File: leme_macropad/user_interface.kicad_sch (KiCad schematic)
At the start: 31 parts, among them J1 OLED display, SW1 SW_Push, SW2 SW_Push, SW3 SW_Push, SW4 RotaryEncoder_Switch, SW5 SW_Push, SW6 SW_Push, SW7 SW_Push, SW8 SW_Push, SW9 SW_Push

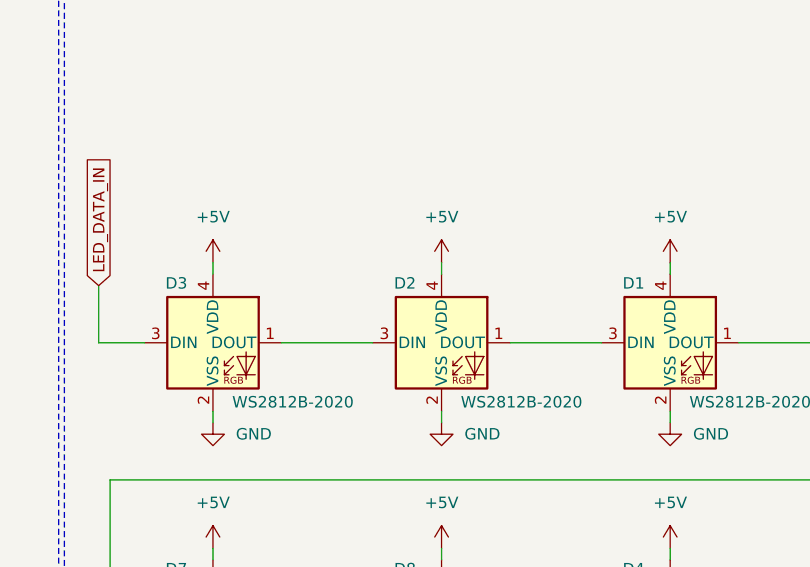
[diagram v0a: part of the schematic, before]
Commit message: Reorders ws2812 LEDs
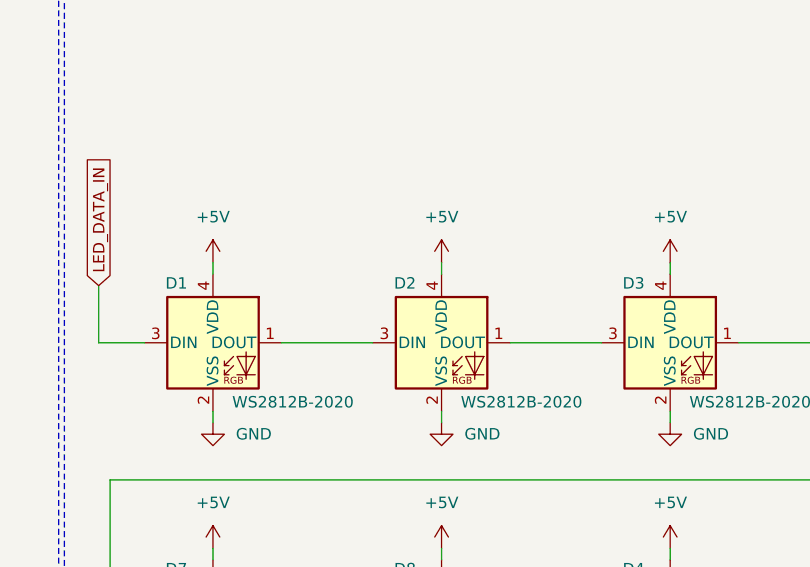
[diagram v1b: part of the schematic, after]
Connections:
- net LED_DATA_IN: now also D1.3 (DIN); no longer D3.3 (DIN)
- net at D3.1 (DOUT): now also D6.3 (DIN); no longer D2.3 (DIN)
- net at D1.1 (DOUT): now also D2.3 (DIN); no longer D6.3 (DIN)
- net at D2.1 (DOUT): now also D3.3 (DIN); no longer D1.3 (DIN)
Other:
- moved on the sheet: D1, D3
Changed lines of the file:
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@@
 	(symbol
 		(lib_id "LED:WS2812B-2020")
-		(at 190.5 63.5 0)
+		(at 241.3 63.5 0)
 		(unit 1)
 		(exclude_from_sim no)
@@
 		(dnp no)
 		(property "Reference" "D3"
-			(at 186.436 56.896 0)
+			(at 237.236 56.896 0)
 			(effects
 				(font
@@
 		)
 		(property "Value" "WS2812B-2020"
-			(at 199.39 70.104 0)
+			(at 250.19 70.104 0)
 			(effects
 				(font
@@
 		)
 		(property "Footprint" "LED_SMD:LED_WS2812B-2020_PLCC4_2.0x2.0mm"
-			(at 191.77 71.12 0)
+			(at 242.57 71.12 0)
 			(effects
 				(font
@@
 		)
 		(property "Datasheet" "https://cdn-shop.adafruit.com/product-files/4684/4684_WS2812B-2020_V1.3_EN.pdf"
-			(at 193.04 73.025 0)
+			(at 243.84 73.025 0)
 			(effects
 				(font
@@
 		)
 		(property "Description" "RGB LED with integrated controller, 2.0 x 2.0 mm, 12 mA"
-			(at 190.5 63.5 0)
+			(at 241.3 63.5 0)
 			(effects
 				(font
@@
 	(symbol
 		(lib_id "LED:WS2812B-2020")
-		(at 241.3 63.5 0)
+		(at 190.5 63.5 0)
 		(unit 1)
 		(exclude_from_sim no)
@@
 		(dnp no)
 		(property "Reference" "D1"
-			(at 237.236 56.896 0)
+			(at 186.436 56.896 0)
 			(effects
 				(font
@@
 		)
 		(property "Value" "WS2812B-2020"
-			(at 250.19 70.104 0)
+			(at 199.39 70.104 0)
 			(effects
 				(font
@@
 		)
 		(property "Footprint" "LED_SMD:LED_WS2812B-2020_PLCC4_2.0x2.0mm"
-			(at 242.57 71.12 0)
+			(at 191.77 71.12 0)
 			(effects
 				(font
@@
 		)
 		(property "Datasheet" "https://cdn-shop.adafruit.com/product-files/4684/4684_WS2812B-2020_V1.3_EN.pdf"
-			(at 243.84 73.025 0)
+			(at 193.04 73.025 0)
 			(effects
 				(font
@@
 		)
 		(property "Description" "RGB LED with integrated controller, 2.0 x 2.0 mm, 12 mA"
-			(at 241.3 63.5 0)
-			(effects
-				(font
+			(at 190.5 63.5 0)
+			(effects
+				(font

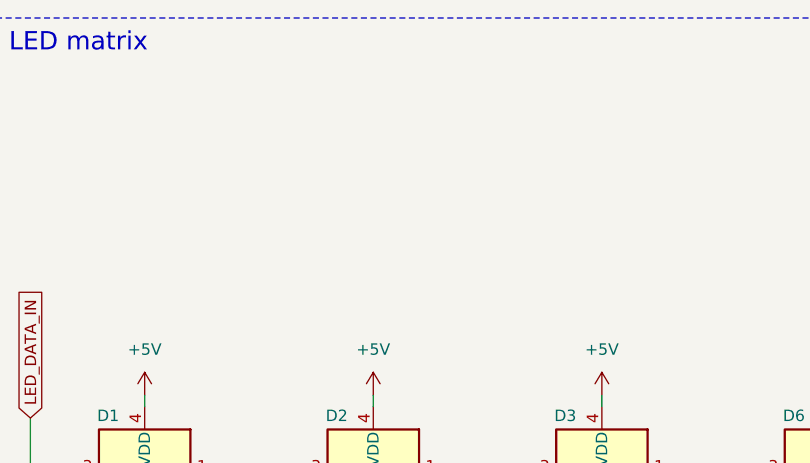
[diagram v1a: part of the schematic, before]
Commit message: Adds pull-up resistor footprint (component marked as DNP) to the LED data line
QMK has a open-drain WS2812 driver[1], which we can potentially use to
drive the LEDs at 5V. The issue is that, in theory, the RP2040 is not 5V
tolerant, and the QMK docs are very specific about this needing to be
the case. That's why the component is marked as "Do Not Populate", and
we'll leave the footprint there for experimentation.

[1]: https://docs.qmk.fm/drivers/ws2812#open-drain-circuit
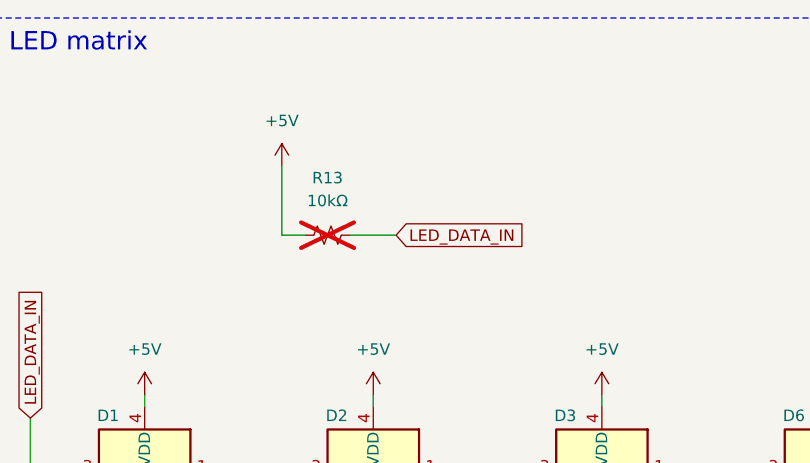
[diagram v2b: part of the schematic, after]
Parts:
- added R13: 10kΩ, Resistor_SMD:R_0402_1005Metric_Pad0.72x0.64mm_HandSolder, symbol Device:R_Small_US
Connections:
- net +5V: now also R13.1
- net LED_DATA_IN: now also R13.2
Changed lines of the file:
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@@
 	(wire
 		(pts
+			(xy 205.74 36.83) (xy 208.28 36.83)
+		)
+		(stroke
+			(width 0)
+			(type default)
+		)
+	)
+	(wire
+		(pts
 			(xy 60.96 95.25) (xy 87.63 95.25)
 		)
@@
 	(wire
 		(pts
+			(xy 205.74 29.21) (xy 205.74 36.83)
+		)
+		(stroke
+			(width 0)
+			(type default)
+		)
+	)
+	(wire
+		(pts
 			(xy 95.25 172.72) (xy 100.33 172.72)
 		)
@@
 	(wire
 		(pts
+			(xy 213.36 36.83) (xy 218.44 36.83)
+		)
+		(stroke
+			(width 0)
+			(type default)
+		)
+	)
+	(wire
+		(pts
 			(xy 60.96 115.57) (xy 63.5 115.57)
 		)
@@
 		)
 	)
+	(global_label "LED_DATA_IN"
+		(shape input)
+		(at 218.44 36.83 0)
+		(fields_autoplaced yes)
+		(effects
+			(font
+				(size 1.27 1.27)
+			)
+			(justify left)
+		)
+		(property "Intersheetrefs" "${INTERSHEET_REFS}"
+			(at 233.1576 36.83 0)
+			(effects
+				(font
+					(size 1.27 1.27)
+				)
+				(justify left)
+				(hide yes)
+			)
+		)
+	)
 	(global_label "I2C0_SDA"
 		(shape input)
@@
 	)
 	(symbol
+		(lib_id "power:+5V")
+		(at 205.74 29.21 0)
+		(unit 1)
+		(exclude_from_sim no)
+		(in_bom yes)
+		(on_board yes)
+		(dnp no)
+		(fields_autoplaced yes)
+		(property "Reference" "#PWR062"
+			(at 205.74 33.02 0)
+			(effects
+				(font
+					(size 1.27 1.27)
+				)
+				(hide yes)
+			)
+		)
+		(property "Value" "+5V"
+			(at 205.74 24.13 0)
+			(effects
+				(font
+					(size 1.27 1.27)
+				)
+			)
+		)
+		(property "Footprint" ""
+			(at 205.74 29.21 0)
+			(effects
+				(font
+					(size 1.27 1.27)
+				)
+				(hide yes)
+			)
+		)
+		(property "Datasheet" ""
+			(at 205.74 29.21 0)
+			(effects
+				(font
+					(size 1.27 1.27)
+				)
+				(hide yes)
+			)
+		)
+		(property "Description" "Power symbol creates a global label with name \"+5V\""
+			(at 205.74 29.21 0)
+			(effects
+				(font
+					(size 1.27 1.27)
+				)
+				(hide yes)
+			)
+		)
+		(pin "1"
+		)
+		(instances
+			(project "leme_macropad"
+				(path "/a37365a2-c635-4451-9354-78f9e753d687/b6fad1bd-9b8b-42cb-b41f-ac701051e19c"
+					(reference "#PWR062")
+					(unit 1)
+				)
+			)
+		)
+	)
+	(symbol
 		(lib_id "Device:D_Small")
 		(at 34.29 90.17 90)
@@
 					(unit 1)
 				)
+			)
+		)
+	)
+	(symbol
+		(lib_id "Device:R_Small_US")
+		(at 210.82 36.83 90)
+		(unit 1)
+		(exclude_from_sim no)
+		(in_bom yes)
+		(on_board yes)
+		(dnp yes)
+		(fields_autoplaced yes)
+		(property "Reference" "R13"
+			(at 210.82 30.48 90)
+			(effects
+				(font
+					(size 1.27 1.27)
+				)
+			)
+		)
+		(property "Value" "10kΩ"
+			(at 210.82 33.02 90)
+			(effects
+				(font
+					(size 1.27 1.27)
+				)
+			)
+		)
+		(property "Footprint" "Resistor_SMD:R_0402_1005Metric_Pad0.72x0.64mm_HandSolder"
+			(at 210.82 36.83 0)
+			(effects
+				(font
+					(size 1.27 1.27)
+				)
+				(hide yes)
+			)
+		)
+		(property "Datasheet" "~"
+			(at 210.82 36.83 0)
+			(effects
+				(font
+					(size 1.27 1.27)
+				)
+				(hide yes)
+			)
+		)
+		(property "Description" "Resistor, small US symbol"
+			(at 210.82 36.83 0)
+			(effects
+				(font
+					(size 1.27 1.27)
+				)
+				(hide yes)
+			)
+		)
+		(pin "1"
+		)
+		(pin "2"
+		)
+		(instances
+			(project "leme_macropad"
+				(path "/a37365a2-c635-4451-9354-78f9e753d687/b6fad1bd-9b8b-42cb-b41f-ac701051e19c"
+					(reference "R13")
+					(unit 1)
+				)

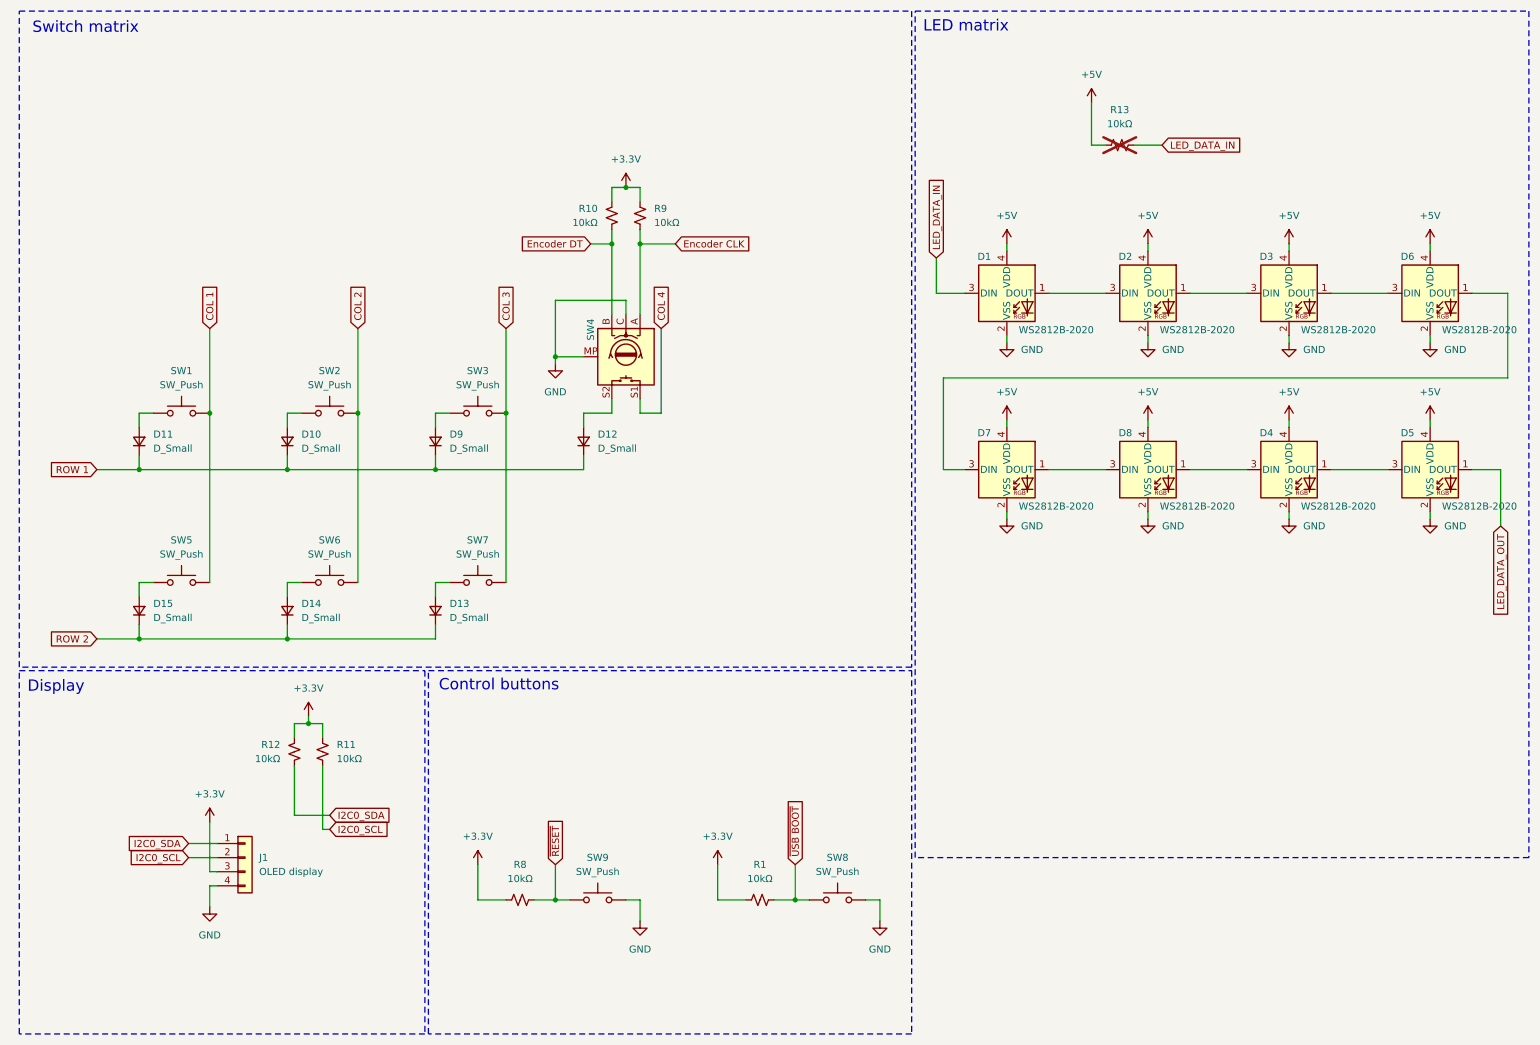
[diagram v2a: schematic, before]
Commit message: Geographically reanotates component designators
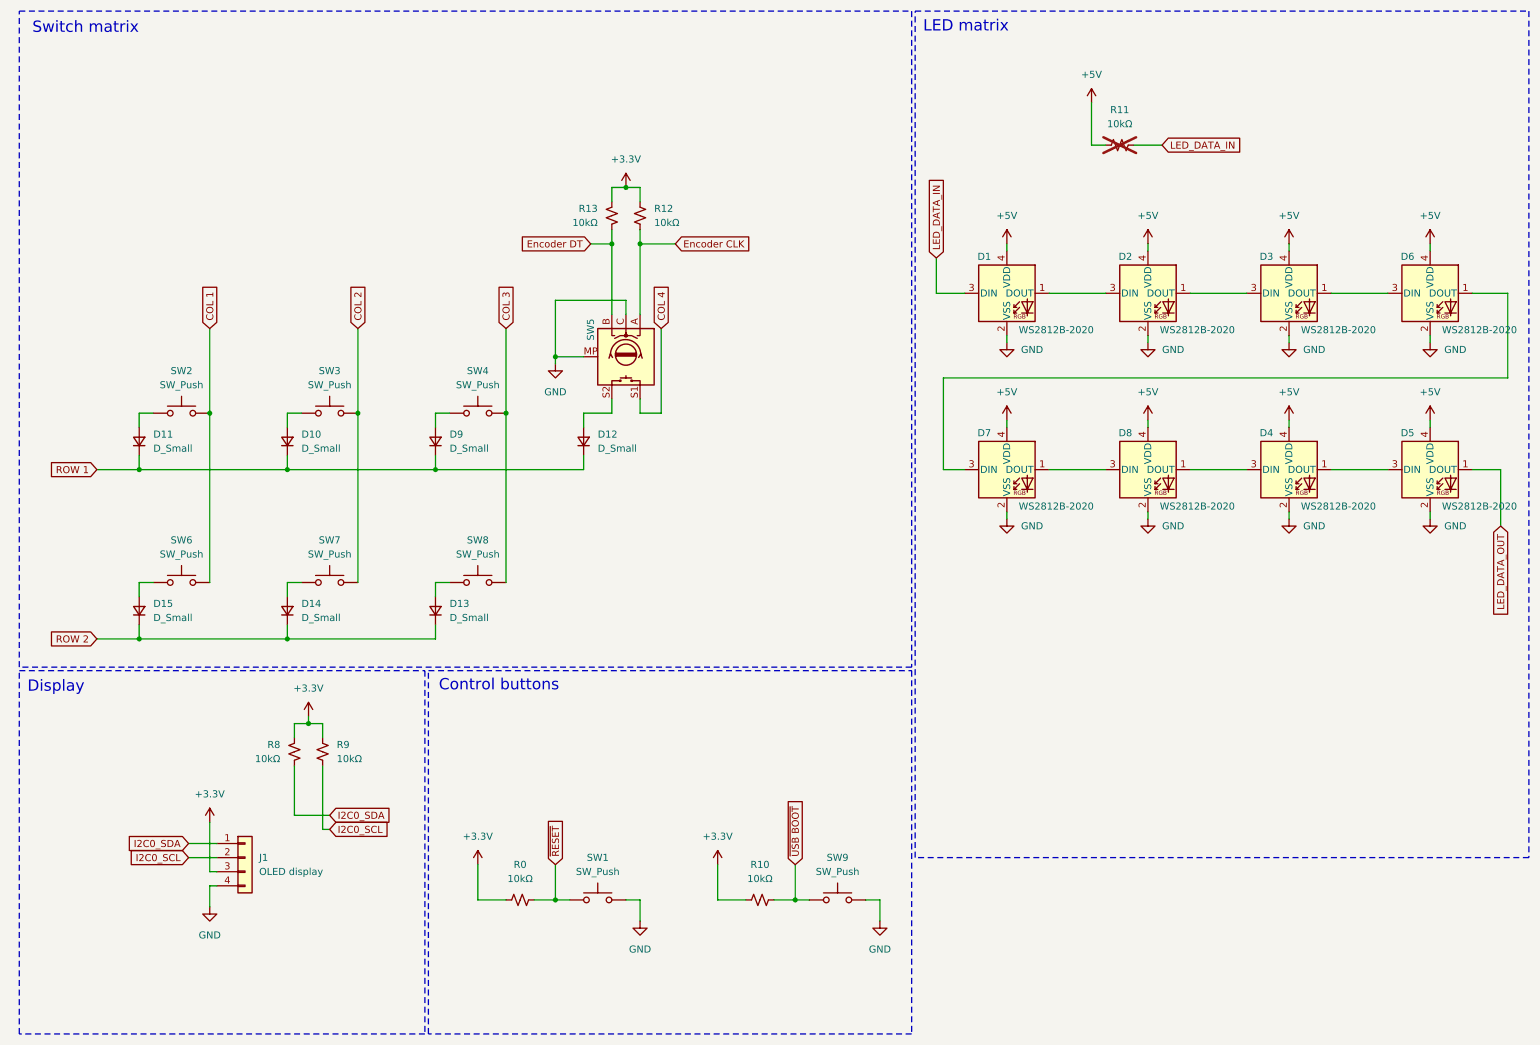
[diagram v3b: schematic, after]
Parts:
- renumbered R8 to R0, R1 to R10, R13 to R11, R9 to R12, R10 to R13, R12 to R8, R11 to R9, SW9 to SW1, SW1 to SW2, SW2 to SW3, SW3 to SW4, SW4 to SW5, SW5 to SW6, SW6 to SW7, SW7 to SW8, SW8 to SW9
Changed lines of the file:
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@@
 		(dnp no)
 		(fields_autoplaced yes)
-		(property "Reference" "R11"
+		(property "Reference" "R9"
 			(at 69.85 144.7799 0)
 			(effects
@@
 			(project "leme_macropad"
 				(path "/a37365a2-c635-4451-9354-78f9e753d687/b6fad1bd-9b8b-42cb-b41f-ac701051e19c"
-					(reference "R11")
+					(reference "R9")
 					(unit 1)
 				)
@@
 		(dnp no)
 		(fields_autoplaced yes)
-		(property "Reference" "SW8"
+		(property "Reference" "SW9"
 			(at 160.02 165.1 0)
 			(effects
@@
 			(project "leme_macropad"
 				(path "/a37365a2-c635-4451-9354-78f9e753d687/b6fad1bd-9b8b-42cb-b41f-ac701051e19c"
-					(reference "SW8")
+					(reference "SW9")
 					(unit 1)
 				)
@@
 		(on_board yes)
 		(dnp no)
-		(property "Reference" "R12"
+		(property "Reference" "R8"
 			(at 59.69 144.7799 0)
 			(effects
@@
 			(project "leme_macropad"
 				(path "/a37365a2-c635-4451-9354-78f9e753d687/b6fad1bd-9b8b-42cb-b41f-ac701051e19c"
-					(reference "R12")
+					(reference "R8")
 					(unit 1)
 				)
@@
 		(dnp no)
 		(fields_autoplaced yes)
-		(property "Reference" "R9"
+		(property "Reference" "R12"
 			(at 127 48.2599 0)
 			(effects
@@
 			(project "leme_macropad"
 				(path "/a37365a2-c635-4451-9354-78f9e753d687/b6fad1bd-9b8b-42cb-b41f-ac701051e19c"
-					(reference "R9")
+					(reference "R12")
 					(unit 1)
 				)
@@
 		(dnp no)
 		(fields_autoplaced yes)
-		(property "Reference" "R1"
+		(property "Reference" "R10"
 			(at 146.05 166.37 90)
 			(effects
@@
 			(project "leme_macropad"
 				(path "/a37365a2-c635-4451-9354-78f9e753d687/b6fad1bd-9b8b-42cb-b41f-ac701051e19c"
-					(reference "R1")
+					(reference "R10")
 					(unit 1)
 				)
@@
 		(on_board yes)
 		(dnp no)
-		(property "Reference" "SW4"
+		(property "Reference" "SW5"
 			(at 115.57 68.072 0)
 			(effects
@@
 			(project "leme_macropad"
 				(path "/a37365a2-c635-4451-9354-78f9e753d687/b6fad1bd-9b8b-42cb-b41f-ac701051e19c"
-					(reference "SW4")
+					(reference "SW5")
 					(unit 1)
 				)
@@
 		(dnp no)
 		(fields_autoplaced yes)
-		(property "Reference" "SW5"
+		(property "Reference" "SW6"
 			(at 41.91 107.95 0)
 			(effects
@@
 			(project "leme_macropad"
 				(path "/a37365a2-c635-4451-9354-78f9e753d687/b6fad1bd-9b8b-42cb-b41f-ac701051e19c"
-					(reference "SW5")
+					(reference "SW6")
 					(unit 1)
 				)
@@
 		(dnp no)
 		(fields_autoplaced yes)
-		(property "Reference" "SW9"
+		(property "Reference" "SW1"
 			(at 116.84 165.1 0)
 			(effects
@@
 			(project "leme_macropad"
 				(path "/a37365a2-c635-4451-9354-78f9e753d687/b6fad1bd-9b8b-42cb-b41f-ac701051e19c"
-					(reference "SW9")
+					(reference "SW1")
 					(unit 1)
 				)
@@
 		(dnp no)
 		(fields_autoplaced yes)
-		(property "Reference" "SW6"
+		(property "Reference" "SW7"
 			(at 68.58 107.95 0)
 			(effects
@@
 			(project "leme_macropad"
 				(path "/a37365a2-c635-4451-9354-78f9e753d687/b6fad1bd-9b8b-42cb-b41f-ac701051e19c"
-					(reference "SW6")
+					(reference "SW7")
 					(unit 1)
 				)
@@
 		(dnp no)
 		(fields_autoplaced yes)
-		(property "Reference" "SW3"
+		(property "Reference" "SW4"
 			(at 95.25 77.47 0)
 			(effects
@@
 			(project "leme_macropad"
 				(path "/a37365a2-c635-4451-9354-78f9e753d687/b6fad1bd-9b8b-42cb-b41f-ac701051e19c"
-					(reference "SW3")
+					(reference "SW4")
 					(unit 1)
 				)
@@
 		(dnp no)
 		(fields_autoplaced yes)
-		(property "Reference" "SW1"
+		(property "Reference" "SW2"
 			(at 41.91 77.47 0)
 			(effects
@@
 			(project "leme_macropad"
 				(path "/a37365a2-c635-4451-9354-78f9e753d687/b6fad1bd-9b8b-42cb-b41f-ac701051e19c"
-					(reference "SW1")
+					(reference "SW2")
 					(unit 1)
 				)
@@
 		(dnp yes)
 		(fields_autoplaced yes)
-		(property "Reference" "R13"
+		(property "Reference" "R11"
 			(at 210.82 30.48 90)
 			(effects
@@
 			(project "leme_macropad"
 				(path "/a37365a2-c635-4451-9354-78f9e753d687/b6fad1bd-9b8b-42cb-b41f-ac701051e19c"
-					(reference "R13")
+					(reference "R11")
 					(unit 1)
 				)
@@
 		(on_board yes)
 		(dnp no)
-		(property "Reference" "R10"
+		(property "Reference" "R13"
 			(at 116.84 48.2599 0)
 			(effects
@@
 			(project "leme_macropad"
 				(path "/a37365a2-c635-4451-9354-78f9e753d687/b6fad1bd-9b8b-42cb-b41f-ac701051e19c"
-					(reference "R10")
+					(reference "R13")
 					(unit 1)
 				)
@@
 		(dnp no)
 		(fields_autoplaced yes)
-		(property "Reference" "SW7"
+		(property "Reference" "SW8"
 			(at 95.25 107.95 0)
 			(effects
@@
 			(project "leme_macropad"
 				(path "/a37365a2-c635-4451-9354-78f9e753d687/b6fad1bd-9b8b-42cb-b41f-ac701051e19c"
-					(reference "SW7")
+					(reference "SW8")
 					(unit 1)
 				)
@@
 		(dnp no)
 		(fields_autoplaced yes)
-		(property "Reference" "SW2"
+		(property "Reference" "SW3"
 			(at 68.58 77.47 0)
 			(effects
@@
 			(project "leme_macropad"
 				(path "/a37365a2-c635-4451-9354-78f9e753d687/b6fad1bd-9b8b-42cb-b41f-ac701051e19c"
-					(reference "SW2")
+					(reference "SW3")
 					(unit 1)
 				)
@@
 		(dnp no)
 		(fields_autoplaced yes)
-		(property "Reference" "R8"
+		(property "Reference" "R0"
 			(at 102.87 166.37 90)
 			(effects
@@
 			(project "leme_macropad"
 				(path "/a37365a2-c635-4451-9354-78f9e753d687/b6fad1bd-9b8b-42cb-b41f-ac701051e19c"
-					(reference "R8")
+					(reference "R0")
 					(unit 1)
 				)
